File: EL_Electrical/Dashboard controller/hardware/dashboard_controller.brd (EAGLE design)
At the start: 69.6 x 55.5 mm, 46 parts, among them IC1 MCP2562-E_SN, IC2 MCP2515-I_SO, J1 22-05-7098-09, Q1 BSS138, Q4 BSS138, Q5 BSS138, Q6 BSS138

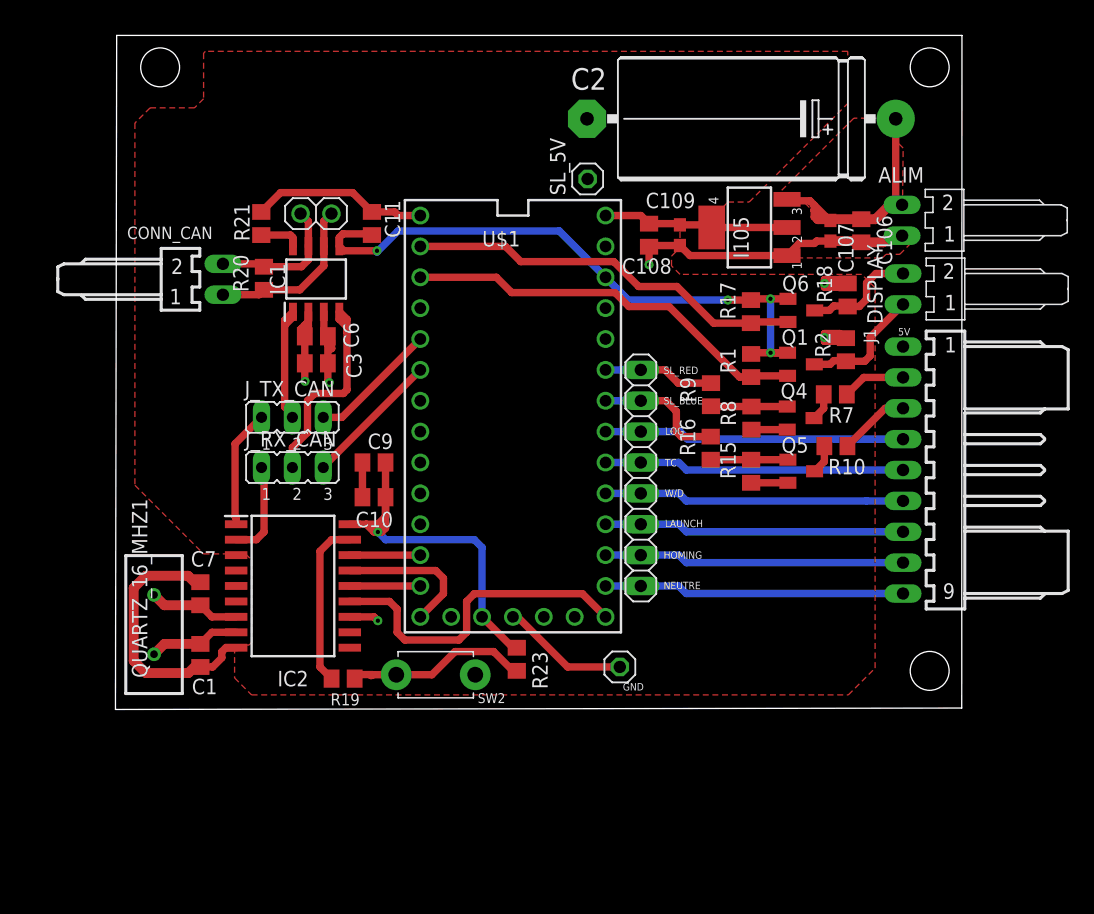
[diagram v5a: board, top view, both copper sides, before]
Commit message: Change connector footprint, LDO regulator (DC linear voltage regulator) position and reduce the size
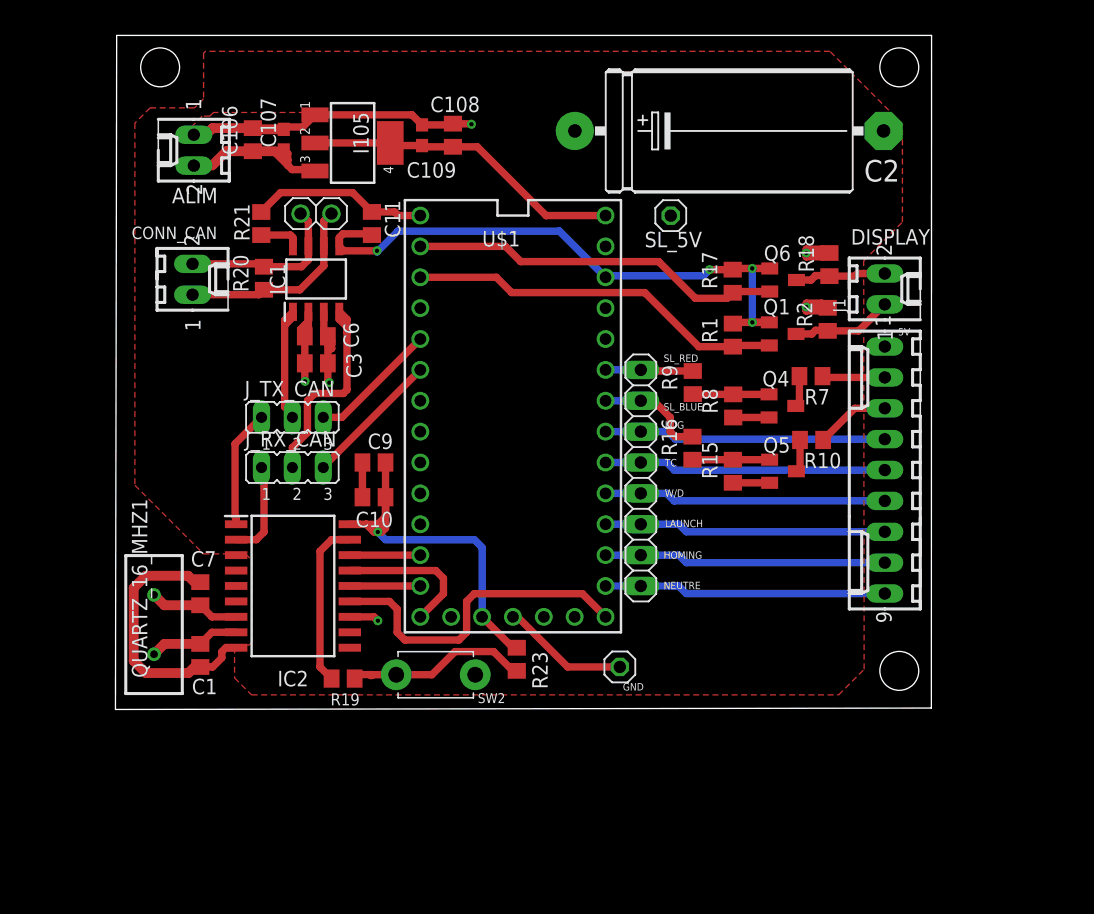
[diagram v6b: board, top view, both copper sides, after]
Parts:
- ALIM, DISPLAY: value 22-05-7028-02 -> 22-27-2021-02; device EP_molex_6410_7395:7395-02 -> con-molex:6410-02
- CONN_CAN: value 22-05-7028-02 -> 22-27-2021-02; device con-molex:7395-02 -> con-molex:6410-02
- J1: value 22-05-7098-09 -> 22-27-2091-09; device con-molex:7395-09 -> con-molex:6410-09
- moved ALIM 58.6 mm to (6.45, 46.0), turned to 90 degrees
- moved C106 50.6 mm to (11.3, 46.9), turned to 90 degrees
- moved C107 45.6 mm to (13.8, 46.9), turned to 90 degrees
- moved I105 33.4 mm to (19.5, 46.6), turned to 270 degrees
- moved C109 22.8 mm to (25.2, 47.2), turned to 270 degrees
- moved C108 18.1 mm to (27.8, 47.2), turned to 90 degrees
- moved SL_5V 7.48 mm to (45.7, 40.6), turned to 180 degrees
- moved Q1 2.92 mm to (54.9, 30.9)
- moved Q6 2.92 mm to (54.9, 35.3)
- moved R1 2.92 mm to (50.8, 30.8)
- moved R17 2.92 mm to (50.8, 35.2)
- moved R18 2.92 mm to (58.7, 36.6)
- moved R2 2.92 mm to (58.6, 32.1)
- moved R7 2.50 mm to (57.2, 27.4)
- moved CONN_CAN 2.50 mm to (6.34, 35.4)
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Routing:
- net +12V: track 21.6 -> 49.5 mm
- net +5V: track 121.1 -> 124.7 mm
- net SC1_3.3V: track 33.7 -> 31.1 mm
- net N$1: track 11.4 -> 13.9 mm
- net N$6: track 13.8 -> 16.3 mm
- net SC2_3.3V: track 32.9 -> 30.7 mm
- net +3V3: track 84.3 -> 82.3 mm
- net SL_RED_PIN: track 9.30 -> 7.38 mm
- net SC1_5V: track 11.2 -> 9.24 mm
- net SC2_5V: track 9.35 -> 7.53 mm
- net SL_BLUE_PIN: track 11.0 -> 9.24 mm
- net W/D_SWITCH_PIN: track 24.7 -> 23.2 mm
- net TC_SWITCH_PIN: track 24.7 -> 23.2 mm
- net NEUTRE_BUTTON: track 24.7 -> 23.2 mm
- net LOG_SWITCH_PIN: track 24.7 -> 23.2 mm
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- removed copper zone on layer 1, net +12V
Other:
- board size 69.6 x 55.5 mm -> 67.1 x 55.5 mm

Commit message: Change connector footprint, LDO regulator (DC linear voltage regulator) position and reduce the size for Gearshift Controller pcb Reduce 1mm for Dashboard Controller pcb
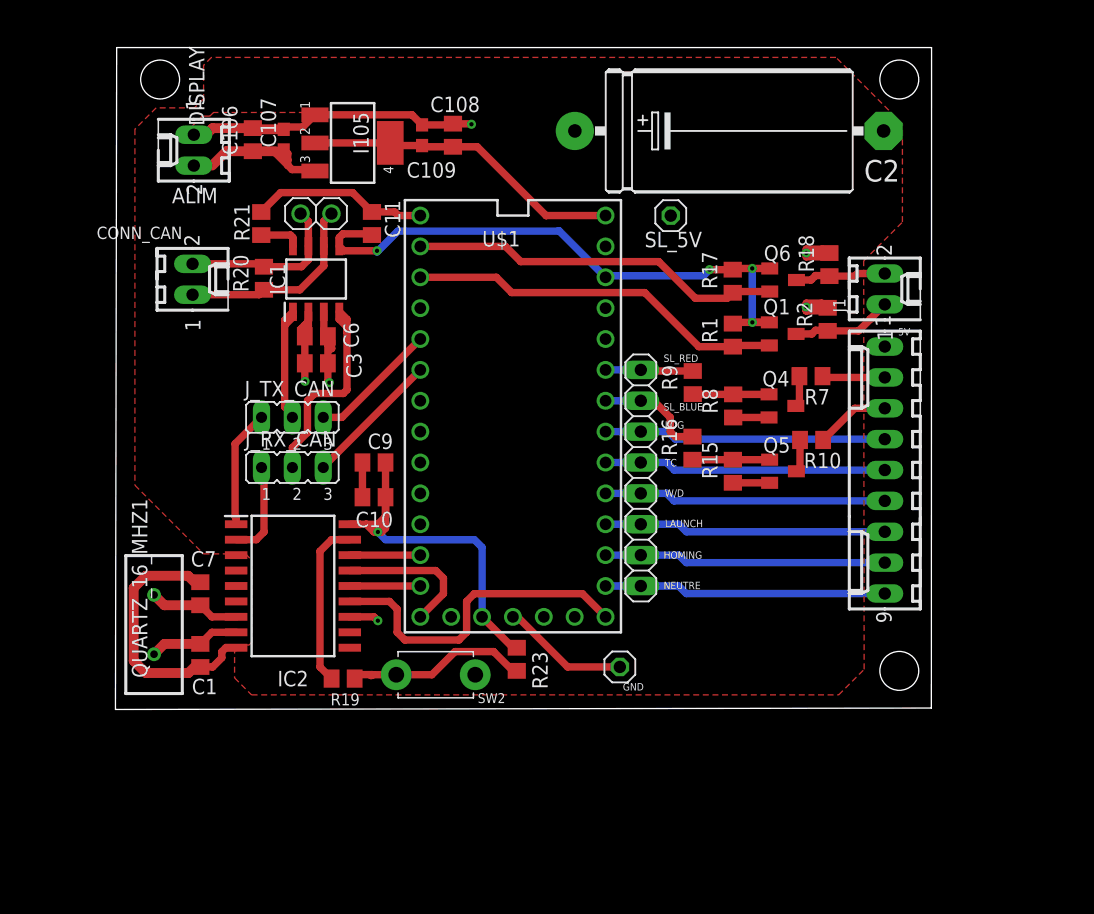
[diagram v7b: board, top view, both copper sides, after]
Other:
- board size 67.1 x 55.5 mm -> 67.1 x 54.5 mm
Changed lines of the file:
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@@
 <setting verticaltext="up"/>
 </settings>
-<grid distance="0.01" unitdist="mm" unit="mm" style="lines" multiple="1" display="no" altdistance="0.1" altunitdist="mm" altunit="mm"/>
+<grid distance="0.5" unitdist="mm" unit="mm" style="lines" multiple="1" display="no" altdistance="0.1" altunitdist="mm" altunit="mm"/>
 <layers>
 <layer number="1" name="Top" color="4" fill="1" visible="yes" active="yes"/>
@@
 <plain>
 <wire x1="0" y1="0" x2="67.13" y2="0.1175" width="0" layer="20"/>
-<wire x1="67.13" y1="0.1175" x2="67.1475" y2="55.46" width="0" layer="20"/>
-<wire x1="67.1475" y1="55.46" x2="0.1" y2="55.46" width="0" layer="20"/>
-<wire x1="0.1" y1="55.46" x2="0" y2="0" width="0" layer="20"/>
-<hole x="64.4925" y="52.8325" drill="3.2"/>
+<wire x1="67.13" y1="0.1175" x2="67.1475" y2="54.46" width="0" layer="20"/>
+<wire x1="67.1475" y1="54.46" x2="0.1" y2="54.46" width="0" layer="20"/>
+<wire x1="0.1" y1="54.46" x2="0" y2="0" width="0" layer="20"/>
+<hole x="64.4925" y="51.8325" drill="3.2"/>
 <hole x="64.4925" y="3.175" drill="3.2"/>
-<hole x="3.675" y="52.8325" drill="3.2"/>
+<hole x="3.675" y="51.8325" drill="3.2"/>
 <text x="45.1" y="28.6" size="0.6096" layer="25">SL_RED</text>
 <text x="45.1" y="24.6" size="0.6096" layer="25">SL_BLUE</text>
@@
 <dimension x1="0.1" y1="48.46" x2="1.3" y2="0" x3="-3.6" y3="24.23" textsize="0.6096" layer="47" dtype="vertical"/>
 <text x="64.4" y="30.775" size="0.6096" layer="25">5V</text>
-<dimension x1="0.1" y1="55.46" x2="-6" y2="0" x3="-8" y3="27.73" textsize="1.778" layer="47" dtype="vertical"/>
 <dimension x1="32.76" y1="41.96" x2="36.52" y2="42.77" x3="34.64" y3="52.54" textsize="1.9304" layer="47" dtype="horizontal"/>
 <dimension x1="0.1" y1="55.46" x2="67.1475" y2="55.46" x3="33.62375" y3="57.35" textsize="1.9304" layer="47" dtype="horizontal"/>
+<dimension x1="0" y1="0" x2="0.1" y2="54.46" x3="-8" y3="27.23" textsize="1.9304" layer="47" dtype="vertical"/>
 </plain>
 <attributes>
@@
 <attribute name="MF" value="MOLEX" x="-7.6275" y="-33.185" size="1.778" layer="27" rot="R270" display="off"/>
 <attribute name="MPN" value="" x="-7.6275" y="-33.185" size="1.778" layer="27" rot="R270" display="off"/>
-<attribute name="NAME" x="1.3249" y="38.7096" size="1.016" layer="25" ratio="10"/>
+<attribute name="NAME" x="-1.5451" y="38.7096" size="1.016" layer="25" ratio="10"/>
 <attribute name="OC_FARNELL" value="unknown" x="-7.6275" y="-33.185" size="1.778" layer="27" rot="R270" display="off"/>
 <attribute name="OC_NEWARK" value="unknown" x="-7.6275" y="-33.185" size="1.778" layer="27" rot="R270" display="off"/>
@@
 <attribute name="MF" value="MOLEX" x="63.3" y="34.6" size="1.778" layer="27" rot="R270" display="off"/>
 <attribute name="MPN" value="" x="63.3" y="34.6" size="1.778" layer="27" rot="R270" display="off"/>
-<attribute name="NAME" x="67.0201" y="39.5179" size="1.27" layer="25" ratio="10" rot="R180"/>
+<attribute name="NAME" x="7.3179" y="48.0299" size="1.27" layer="25" ratio="10" rot="R90"/>
 <attribute name="OC_FARNELL" value="unknown" x="63.3" y="34.6" size="1.778" layer="27" rot="R270" display="off"/>
 <attribute name="OC_NEWARK" value="unknown" x="63.3" y="34.6" size="1.778" layer="27" rot="R270" display="off"/>
@@
 <wire x1="2.5" y1="3" x2="6.005" y2="3" width="0.8128" layer="1"/>
 <polygon width="0.3" layer="1">
-<vertex x="1.6" y="48.25"/>
+<vertex x="1.6" y="47.75"/>
 <vertex x="1.6" y="18.45"/>
 <vertex x="7.25" y="12.8"/>
@@
 <vertex x="64.75" y="40.1"/>
 <vertex x="64.75" y="48.183434375"/>
-<vertex x="58.783434375" y="54.15"/>
-<vertex x="7.4" y="54.15"/>
-<vertex x="7.25" y="54"/>
+<vertex x="59.283434375" y="53.65"/>
+<vertex x="7.9" y="53.65"/>
+<vertex x="7.25" y="53"/>
 <vertex x="7.25" y="50.25"/>
 <vertex x="6.5" y="49.5"/>
-<vertex x="2.85" y="49.5"/>
+<vertex x="3.35" y="49.5"/>
 </polygon>
 <polygon width="0.6096" layer="2">
-<vertex x="57.8870125" y="54.617371875"/>
-<vertex x="57.897503125" y="54.625"/>
-<vertex x="7.75" y="54.625"/>
-<vertex x="7.375" y="54.25"/>
+<vertex x="59.373665625" y="53.25"/>
+<vertex x="7.375" y="53.25"/>
 <vertex x="7.375" y="50.125"/>
 <vertex x="6.625" y="49.375"/>
-<vertex x="3" y="49.375"/>
-<vertex x="1.75" y="48.125"/>
+<vertex x="3.5" y="49.375"/>
+<vertex x="1.75" y="47.625"/>
 <vertex x="1.75" y="1.625"/>
 <vertex x="2.625" y="0.75"/>
@@
 <vertex x="61.4" y="36.78"/>
 <vertex x="64.89" y="40.27"/>
-<vertex x="64.89" y="48.05"/>
-<vertex x="58.319659375" y="54.620340625"/>
-<vertex x="57.8870125" y="54.617371875"/>
+<vertex x="64.89" y="47.55"/>
+<vertex x="59.319659375" y="53.120340625"/>
+<vertex x="59.373665625" y="53.25"/>
 </polygon>
 <contactref element="GND" pad="1"/>
@@
 <vertex x="61.39" y="2.79"/>
 <vertex x="61.39" y="51.26"/>
-<vertex x="58.667409375" y="53.982590625"/>
-<vertex x="7.4" y="53.6"/>
+<vertex x="58.66370625" y="53.98629375"/>
+<vertex x="7.4" y="53.60373125"/>
 <vertex x="7.4" y="50.15"/>
-<vertex x="6.6" y="49.35"/>
-<vertex x="2.95" y="49.35"/>
-<vertex x="1.6" y="47.95"/>
+<vertex x="6.1" y="48.85"/>
+<vertex x="2.95" y="48.85"/>
+<vertex x="1.6" y="47.45"/>
 </polygon>
 <contactref element="R2" pad="2"/>
